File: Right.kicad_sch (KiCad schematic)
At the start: 196 parts, among them J1 USB_C_Receptacle_USB2.0, J2 USB_C_Receptacle_USB2.0, J3 AVR-ISP-6, Q1 DMN2041L, Q2 DMN2041L, SW1 SW_Push, SW10 SW_Push, SW11 SW_Push, SW12 SW_Push, SW13 SW_Push, SW14 SW_Push, SW15 SW_Push, SW17 SW_Push, SW18 SW_Push, SW2 SW_Push, SW20 SW_Push, SW21 SW_Push, SW23 SW_Push, SW24 SW_Push, SW25 SW_Push, SW27 SW_Push, SW28 SW_Push, SW3 SW_Push, SW30 SW_Push, SW31 SW_Push, SW32 SW_Push, SW33 SW_Push, SW34 SW_Push, SW35 SW_Push, SW36 SW_Push, SW37 SW_Push, SW38 SW_Push, SW39 SW_Push, SW4 SW_Push, SW40 SW_Push, SW41 SW_Push, SW42 SW_Push, SW43 SW_Push, SW44 SW_Push, SW45 SW_Push, SW46 SW_Push, SW47 SW_Push, SW5 SW_Push, SW6 SW_Push, SW7 SW_Push, SW8 SW_Push, SW9 SW_Push, U1 ATmega32U4-A, Y1 16MHz

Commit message: replaced LEDs with RGBs, and started the PCB for keyboard
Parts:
- removed C1, C2, C7: .1uF, symbol Device:C_Small
- removed C3, C5: 22pF, symbol Device:C_Small
- removed C4: 1uF, symbol Device:C_Small
- removed C6: 10uf, symbol Device:C_Small
- removed D1, D11, D14, D17, D18, D19, D2, D20, D3, D31, D33, D34, D35, D39, D40, D44, D46, D48, D50, D52, D56, D61, D62, D63, D64, D67, D7, D72, D73, D74, D75, D76, D79, D8, D82, D83, D85, D86, D88, D9, D91: LED, symbol Device:LED
- removed D10, D16, D22, D23, D25, D29, D30, D37, D4, D42, D43, D47, D5, D51, D54, D58, D6, D60, D66, D68, D69, D71, D78, D84, D87, D89, D90: D_Small, symbol Device:D_Small
- removed D21: PRTR5V0U2X, Package_TO_SOT_SMD:SOT-143, symbol Power_Protection:PRTR5V0U2X
- removed F1: 500m, symbol Device:Polyfuse_Small
- removed J1: USB_C_Receptacle_USB2.0, symbol Connector:USB_C_Receptacle_USB2.0
- removed J3: AVR-ISP-6, symbol Connector:AVR-ISP-6
- removed Q1: DMN2041L, Package_TO_SOT_SMD:SOT-23, symbol Transistor_FET:DMN2041L
- removed R1, R11, R12, R13, R14, R15, R17, R18, R19, R20, R24, R25, R27, R28, R29, R3, R30, R33, R35, R36, R37, R38, R39, R4, R40, R41, R42, R43, R45, R46, R47, R48, R49, R5, R50, R52, R53, R54, R6, R7, R9: 470, symbol Device:R_Small
- removed R2, R44: 22, symbol Device:R_Small
- removed R21: 1k, symbol Device:R_Small
- removed R22, R31: 5.1k, symbol Device:R_Small
- removed R23, R34: 10k, symbol Device:R_Small
- removed SW1, SW12, SW15, SW18, SW2, SW20, SW24, SW27, SW3, SW31, SW32, SW34, SW35, SW37, SW39, SW4, SW41, SW42, SW43, SW44, SW46, SW47, SW5, SW6, SW7, SW8, SW9: SW_Push, keyswitches.pretty-2:Kailh_socket_PG1350, symbol Switch:SW_Push
- removed SW28: SW_Push, Button_Switch_SMD:SW_SPST_SKQG_WithStem, symbol Switch:SW_Push
- removed Y1: 16MHz, symbol Device:Crystal_GND24_Small
- added C301, C302: 22pF, Capacitor_SMD:C_0402_1005Metric, symbol Device:C_Small
- added C303: 1uF, Capacitor_SMD:C_0402_1005Metric, symbol Device:C_Small
- added C304, C305, C306: .1uF, Capacitor_SMD:C_0402_1005Metric, symbol Device:C_Small
- added C307: 10uf, Capacitor_SMD:C_0402_1005Metric, symbol Device:C_Small
- added C308, C309, C310, C311, C312, C313, C314, C315, C316, C317, C318, C319, C320, C321, C322, C323, C324, C325, C326, C327, C328, C329, C330, C331, C332, C333, C334, C335, C336, C337, C338, C339, C340, C341, C342, C343, C344, C345, C346, C347, C348: 100nF, Capacitor_SMD:C_0402_1005Metric, symbol Device:C_Small
- added D302: PRTR5V0U2X, Package_TO_SOT_SMD:SOT-143, symbol Power_Protection:PRTR5V0U2X
- added D303, D304, D305, D306, D307, D308, D309, D310, D311, D312, D313, D314, D315, D316, D317, D318, D319, D320, D321, D322, D323, D324, D325, D326, D327, D328, D329, D330, D331, D332, D333, D334, D335, D336, D337, D338, D339, D340, D341, D342, D343: NeoPixel_THT, kicad-keyboard-parts.pretty:LED_RGB_Wuerth-PLCC4_3.2x2.8mm_150141M173100, symbol LED:NeoPixel_THT
- added D346, D347, D349, D350, D351, D352, D353, D354, D355, D356, D357, D358, D359, D360, D362, D374, D375, D376, D377, D378, D379, D380, D381, D382, D383, D384, D385: D_Small, Diode_SMD:D_SOD-123, symbol Device:D_Small
- added F301: 500m, Keebio-Parts:Fuse_0805, symbol Device:Polyfuse_Small
- added FB301: FerriteBead_Small, Inductor_SMD:L_0805_2012Metric_Pad1.15x1.40mm_HandSolder, symbol Device:FerriteBead_Small
- added H301, H302, H303, H304, H305, H306: MountingHole, MountingHole:MountingHole_2.2mm_M2_DIN965_Pad, symbol Mechanical:MountingHole
- added J302: USB_C_Receptacle_USB2.0, Type-C:HRO-TYPE-C-31-M-13, symbol Connector:USB_C_Receptacle_USB2.0
- added J303: AVR-ISP-6, Keebio-Parts:ICSP-Header, symbol Connector:AVR-ISP-6
- added R302, R304: 5.1k, Resistor_SMD:R_0402_1005Metric, symbol Device:R_Small
- added R305: 300, Resistor_SMD:R_0402_1005Metric, symbol Device:R_Small
- added R323, R327: 22, Resistor_SMD:R_0402_1005Metric, symbol Device:R_Small
- added R328, R341: 10k, Resistor_SMD:R_0402_1005Metric, symbol Device:R_Small
- added SW301: SW_Push, Button_Switch_SMD:SW_SPST_SKQG_WithStem, symbol Switch:SW_Push
- added SW304, SW305, SW307, SW308, SW309, SW311, SW312, SW313, SW314, SW316, SW317, SW318, SW320, SW331, SW332, SW333, SW336, SW337, SW338, SW339, SW340, SW341, SW342: SW_Push, keyswitches.pretty-2:Kailh_socket_PG1350, symbol Switch:SW_Push
- added SW310, SW335: SW_Push, keyswitches.pretty-2:Kailh_socket_PG1350_2.25U, symbol Switch:SW_Push
- added SW315: SW_Push, keyswitches.pretty-2:Kailh_socket_PG1350_1.25U, symbol Switch:SW_Push
- added SW334: SW_Push, keyswitches.pretty-2:Kailh_socket_PG1350_1.5U, symbol Switch:SW_Push
- added Y301: 16MHz, Crystal:Crystal_SMD_3225-4Pin_3.2x2.5mm, symbol Device:Crystal_GND24_Small
- D344: renamed from D15; footprint (none) -> Diode_SMD:D_SOD-123
- D345: renamed from D81; footprint (none) -> Diode_SMD:D_SOD-123
- D348: renamed from D12; footprint (none) -> Diode_SMD:D_SOD-123
- D361: renamed from D45; footprint (none) -> Diode_SMD:D_SOD-123
- D363: renamed from D41; footprint (none) -> Diode_SMD:D_SOD-123
- D364: renamed from D26; footprint (none) -> LED_SMD:LED_PLCC_2835
- D365: renamed from D70; footprint (none) -> Diode_SMD:D_SOD-123
- D366: renamed from D27; footprint (none) -> Diode_SMD:D_SOD-123
- D367: renamed from D57; footprint (none) -> Diode_SMD:D_SOD-123
- D368: renamed from D28; footprint (none) -> Diode_SMD:D_SOD-123
- D369: renamed from D80; footprint (none) -> Diode_SMD:D_SOD-123
- D370: renamed from D49; footprint (none) -> Diode_SMD:D_SOD-123
- D371: renamed from D77; footprint (none) -> Diode_SMD:D_SOD-123
- D372: renamed from D13; footprint (none) -> Diode_SMD:D_SOD-123
- D373: renamed from D24; footprint (none) -> Diode_SMD:D_SOD-123
- J301: renamed from J2; footprint (none) -> Type-C:HRO-TYPE-C-31-M-13
- R301: renamed from R32; footprint (none) -> Resistor_SMD:R_0402_1005Metric
- R303: renamed from R51; footprint (none) -> Resistor_SMD:R_0402_1005Metric
- R345: renamed from R26; footprint (none) -> Resistor_SMD:R_0402_1005Metric
- R346: renamed from R16; footprint (none) -> Resistor_SMD:R_0402_1005Metric
- R353: renamed from R8; footprint (none) -> Resistor_SMD:R_0402_1005Metric
- R354: renamed from R10; footprint (none) -> Resistor_SMD:R_0402_1005Metric
- SW329: renamed from SW36; footprint keyswitches.pretty-2:Kailh_socket_PG1350 -> keyswitches.pretty-2:Kailh_socket_PG1350_1.75U
- gave numbers to parts that had none: 1
- renumbered Q2 to Q302, SW25 to SW302, SW23 to SW303, SW13 to SW306, SW38 to SW319, SW11 to SW321, SW33 to SW322, SW10 to SW323, SW17 to SW324, SW14 to SW325, SW45 to SW326, SW21 to SW327, SW30 to SW328, SW40 to SW330, U1 to U301
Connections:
- net +5V: now also C304.1, C305.1, C306.1, C307.1, C308.2, C309.2, C310.2, C311.2, C312.1, C312.2, C313.2, C314.2, C315.2, C316.2, C317.2, C318.2, C319.2, C320.2, C321.2, C322.2, C323.2, C324.2, C325.2, C326.2, C327.2, C328.2, C329.2, C330.2, C331.2, C332.2, C333.2, C334.2, C335.2, C336.2, C337.2, C338.2, C339.2, C340.2, C341.2, C342.2, C343.2, C344.2, C345.2, C346.2, C347.1, C347.2, C348.2, D303.3 (VDD), D304.3 (VDD), D305.3 (VDD), D306.3 (VDD), D307.3 (VDD), D308.3 (VDD), D309.3 (VDD), D310.3 (VDD), D311.3 (VDD), D312.3 (VDD), D313.3 (VDD), D314.3 (VDD), D315.3 (VDD), D316.3 (VDD), D317.3 (VDD), D318.3 (VDD), D319.3 (VDD), D320.3 (VDD), D321.3 (VDD), D322.3 (VDD), D323.3 (VDD), D324.3 (VDD), D325.3 (VDD), D326.3 (VDD), D327.3 (VDD), D328.3 (VDD), D329.3 (VDD), D330.3 (VDD), D331.3 (VDD), D332.3 (VDD), D333.3 (VDD), D334.2 (GND), D334.3 (VDD), D335.3 (VDD), D336.3 (VDD), D337.3 (VDD), D338.3 (VDD), D339.3 (VDD), D340.3 (VDD), D341.3 (VDD), D342.3 (VDD), D343.3 (VDD), F301.2, J303.2 (VCC), R328.1
- net COL_0: now also SW304.2, SW305.2
- net COL_1: now also SW307.2, SW308.2, SW309.2, SW310.2
- net COL_2: now also SW311.2, SW312.2, SW313.2, SW314.2, SW315.2
- net COL_3: now also SW316.2, SW317.2, SW318.2, SW320.2
- net D+: now also D302.3 (I/O2), J302.A6 (D+), J302.B6 (D+), R327.1
- net D-: now also D302.2 (I/O1), J302.A7 (D-), J302.B7 (D-), R323.1
- net DATA_2: now also D301.2 (I/O1)
- net GND: now also C301.1, C302.2, C303.2, C304.2, C305.2, C306.2, C307.2, C308.1, C309.1, C310.1, C311.1, C313.1, C314.1, C315.1, C316.1, C317.1, C318.1, C319.1, C320.1, C321.1, C322.1, C323.1, C324.1, C325.1, C326.1, C327.1, C328.1, C329.1, C330.1, C331.1, C332.1, C333.1, C334.1, C335.1, C336.1, C337.1, C338.1, C339.1, C340.1, C341.1, C342.1, C343.1, C344.1, C345.1, C346.1, C348.1, D302.1 (GND), D303.2 (GND), D304.2 (GND), D305.2 (GND), D306.2 (GND), D307.2 (GND), D308.2 (GND), D309.2 (GND), D310.2 (GND), D311.2 (GND), D312.2 (GND), D313.2 (GND), D314.2 (GND), D315.2 (GND), D316.2 (GND), D317.2 (GND), D318.2 (GND), D319.2 (GND), D320.2 (GND), D321.2 (GND), D322.2 (GND), D323.2 (GND), D324.2 (GND), D325.2 (GND), D326.2 (GND), D327.2 (GND), D328.2 (GND), D329.2 (GND), D330.2 (GND), D331.2 (GND), D332.2 (GND), D333.2 (GND), D335.2 (GND), D336.2 (GND), D337.2 (GND), D338.2 (GND), D339.2 (GND), D340.2 (GND), D341.2 (GND), D342.2 (GND), D343.2 (GND), FB301.2, J302.A1 (GND), J302.A12 (GND), J302.B1 (GND), J302.B12 (GND), J303.6 (GND), R302.2, R304.2, R341.2, SW301.1, Y301.2, Y301.4
- net MISO: now also J303.1 (MISO)
- net MOSI: now also J303.4 (MOSI)
- net ROW_0: now also D352.1 (K), D357.1 (K), D362.1 (K), D380.1 (K), D385.1 (K)
- net ROW_1: now also D347.1 (K), D351.1 (K), D356.1 (K), D379.1 (K), D384.1 (K)
- net ROW_2: now also D346.1 (K), D350.1 (K), D355.1 (K), D360.1 (K), D378.1 (K), D383.1 (K)
- net ROW_3: now also D349.1 (K), D354.1 (K), D359.1 (K), D375.1 (K), D377.1 (K), D382.1 (K)
- net ROW_4: now also D353.1 (K), D358.1 (K), D374.1 (K), D376.1 (K), D381.1 (K)
- net RST: now also J303.5 (~{RST}), R328.2, SW301.2
- net SCLK: now also J303.3 (SCK)
- net VCC: now also D302.4 (VCC), F301.1, J302.A4 (VBUS), J302.A9 (VBUS), J302.B4 (VBUS), J302.B9 (VBUS)
- net at U301.16 (XTAL2): now also C302.1, Y301.3
- net at U301.17 (XTAL1): now also C301.2, Y301.1
- net COL_8: now reaches U301.19 (PD1)
- net COL_8: now also SW338.2, SW339.2, SW340.2, SW341.2, SW342.2
- net D_N: now reaches U301.3 (D-)
- net D_N: now also R323.2
- net at U301.33 (~{HWB}/PE2): now also R341.1
- net D_P: now reaches U301.4 (D+)
- net D_P: now also R327.2
- net at U301.6 (UCAP): now also C303.1
- net PWM: no longer names the net of U301.12 (PB7)
- net PWM: now also R305.1
- net ROW_5 renamed COL_6
- net COL_6: now also SW331.2, SW332.2
- net ROW_6 renamed COL_7
- net COL_7: now also SW333.2, SW334.2, SW335.2, SW336.2, SW337.2
- new net: D360.2 (A), SW318.1
- new net: D353.2 (A), SW311.1
- new net: D376.2 (A), SW333.1
- new net: D331.1 (DOUT), D332.4 (DIN)
- new net: D330.1 (DOUT), D331.4 (DIN)
- new net: D362.2 (A), SW320.1
- new net: D338.1 (DOUT), D339.4 (DIN)
- new net: D337.1 (DOUT), D338.4 (DIN)
- new net: J302.A5 (CC1), R304.1
- new net: D319.1 (DOUT), D320.4 (DIN)
- new net: D354.2 (A), SW312.1
- new net: J302.B5 (CC2), R302.1
- new net: D377.2 (A), SW334.1
- new net: D381.2 (A), SW338.1
- new net: D358.2 (A), SW316.1
- new net: D352.2 (A), SW310.1
- new net: D351.2 (A), SW309.1
- new net: D355.2 (A), SW313.1
- new net: D384.2 (A), SW341.1
- new net: D307.1 (DOUT), D308.4 (DIN)
- new net: D306.1 (DOUT), D307.4 (DIN)
- new net: D349.2 (A), SW307.1
- new net: D312.1 (DOUT), D313.4 (DIN)
- new net: D311.1 (DOUT), D312.4 (DIN)
- new net: D329.1 (DOUT), D330.4 (DIN)
- new net: D346.2 (A), SW304.1
- new net: D339.1 (DOUT), D340.4 (DIN)
- new net: D357.2 (A), SW315.1
- new net: D336.1 (DOUT), D337.4 (DIN)
- new net: D340.1 (DOUT), D341.4 (DIN)
- new net: D350.2 (A), SW308.1
- new net: D322.1 (DOUT), D323.4 (DIN)
- new net: D321.1 (DOUT), D322.4 (DIN)
- new net: D382.2 (A), SW339.1
- new net: D359.2 (A), SW317.1
- new net: D378.2 (A), SW335.1
- new net: D380.2 (A), SW337.1
- new net: D305.1 (DOUT), D306.4 (DIN)
- new net: D309.1 (DOUT), D310.4 (DIN)
- new net: D308.1 (DOUT), D309.4 (DIN)
- new net: D385.2 (A), SW342.1
- new net: D315.1 (DOUT), D316.4 (DIN)
- new net: D314.1 (DOUT), D315.4 (DIN)
- new net: D317.1 (DOUT), D318.4 (DIN)
- new net: D316.1 (DOUT), D317.4 (DIN)
- new net: D383.2 (A), SW340.1
- new net: D335.1 (DOUT), D336.4 (DIN)
- new net: D325.1 (DOUT), D326.4 (DIN)
- new net: D324.1 (DOUT), D325.4 (DIN)
- new net: D356.2 (A), SW314.1
- new net: D320.1 (DOUT), D321.4 (DIN)
- new net: D328.1 (DOUT), D329.4 (DIN)
- new net: D327.1 (DOUT), D328.4 (DIN)
- new net: D379.2 (A), SW336.1
- new net: D303.1 (DOUT), D304.4 (DIN)
- new net: D341.1 (DOUT), D342.4 (DIN)
- new net: D374.2 (A), SW331.1
- new net: D313.1 (DOUT), D314.4 (DIN)
- new net: D347.2 (A), SW305.1
- new net: D323.1 (DOUT), D324.4 (DIN)
- new net: D333.1 (DOUT), D334.4 (DIN)
- new net: D332.1 (DOUT), D333.4 (DIN)
- new net: D304.1 (DOUT), D305.4 (DIN)
- new net: D375.2 (A), SW332.1
- new net D211: D310.1 (DOUT), D311.4 (DIN)
- new net D219: D318.1 (DOUT), D319.4 (DIN)
- new net D227: D326.1 (DOUT), D327.4 (DIN)
- new net D235: D334.1 (DOUT), D335.4 (DIN)
- new net D303: D303.4 (DIN), D343.1 (DOUT)
- new net Earth: FB301.1, J302.S1 (SHIELD)
- new net RGB: D343.4 (DIN), R305.2
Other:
- note added: "41 RGB LEDs Matrix"
- note removed: "41 LEDs"
- moved on the sheet: D301, D344, D345, D348, D361, D363, D365, D366, D367, D368, D369, D370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

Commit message: did some more work on the keyboard, played around with the rotary footprint
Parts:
- SW301: footprint Button_Switch_SMD:SW_SPST_SKQG_WithStem -> Keebio-Parts:SW_SPST_TL3342
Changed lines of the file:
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@@
     (property "Reference" "SW301" (id 0) (at 190.5 76.2 0))
     (property "Value" "SW_Push" (id 1) (at 190.5 78.74 0))
-    (property "Footprint" "Button_Switch_SMD:SW_SPST_SKQG_WithStem" (id 2) (at 190.5 78.74 0)
+    (property "Footprint" "Keebio-Parts:SW_SPST_TL3342" (id 2) (at 190.5 78.74 0)
       (effects (font (size 1.27 1.27)) hide)
     )

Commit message: did some routing
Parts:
- removed D301: PRTR5V0U2X, Package_TO_SOT_SMD:SOT-143, symbol Power_Protection:PRTR5V0U2X
- removed D364: LED, LED_SMD:LED_PLCC_2835, symbol Device:LED
- removed J301: USB_C_Receptacle_USB2.0, Type-C:HRO-TYPE-C-31-M-13, symbol Connector:USB_C_Receptacle_USB2.0
- removed Q302: DMN2041L, Package_TO_SOT_SMD:SOT-23, symbol Transistor_FET:DMN2041L
- removed R301, R303: 5.1k, Resistor_SMD:R_0402_1005Metric, symbol Device:R_Small
- removed R345, R346: 4.7K, Resistor_SMD:R_0402_1005Metric, symbol Device:R_Small
- removed R353: 470, Resistor_SMD:R_0402_1005Metric, symbol Device:R_Small
- removed R354: 1k, Resistor_SMD:R_0402_1005Metric, symbol Device:R_Small
- added R1, R2: 4.7K, Resistor_SMD:R_0402_1005Metric, symbol Device:R_Small
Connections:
- net +5V: now also R1.2, R2.2
- net DATA_1: now also U301.20 (PD2), R2.1
- net DATA_2: now also U301.21 (PD3), R1.1
- no-connect marks 10 -> 8
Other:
- note removed: "CAPS LOCK LED"

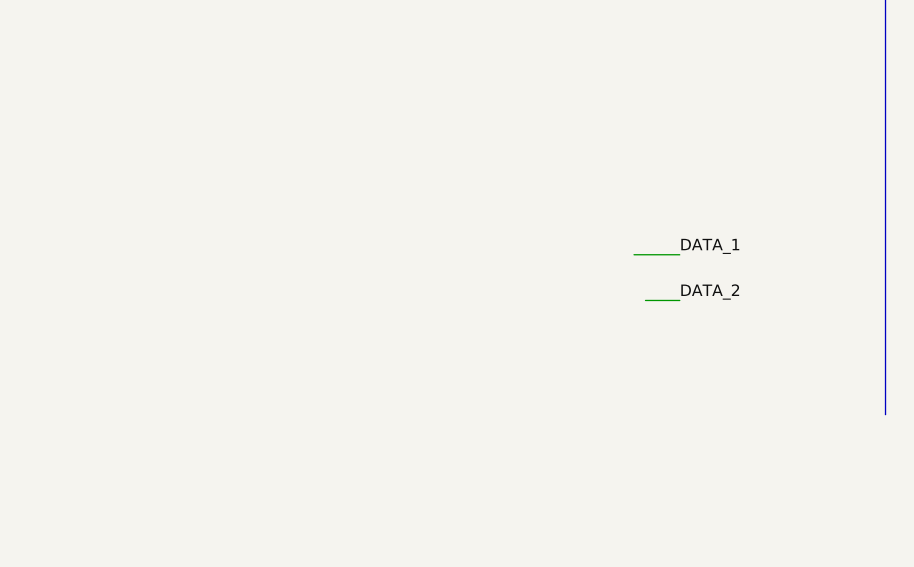
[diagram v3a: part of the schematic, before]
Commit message: placed some i2cs
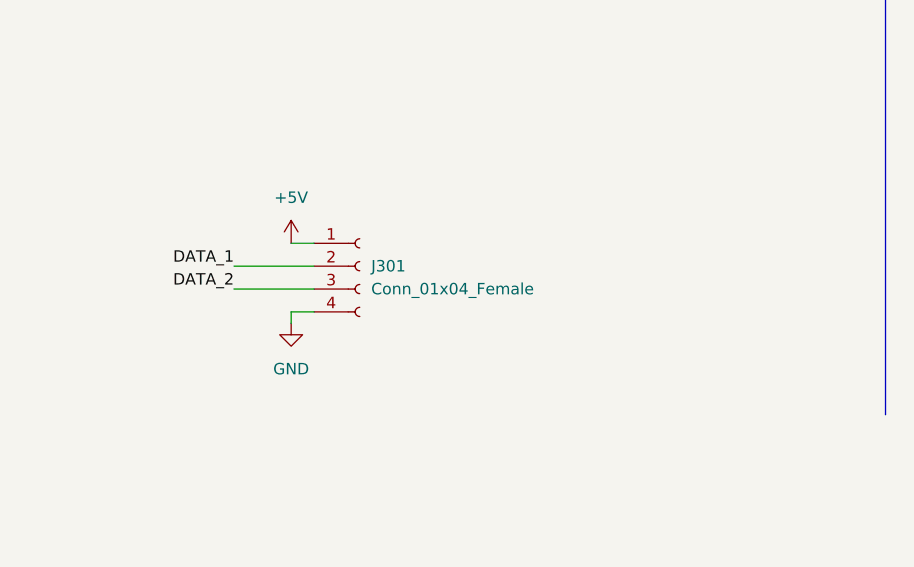
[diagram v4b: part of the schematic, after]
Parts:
- added J301: Conn_01x04_Female, Keebio-Parts:I2C_Breakout, symbol Connector:Conn_01x04_Female
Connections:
- net +5V: now also J301.1 (Pin_1)
- net DATA_1: now also J301.2 (Pin_2)
- net DATA_2: now also J301.3 (Pin_3)
- net GND: now also J301.4 (Pin_4)
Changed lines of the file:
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@@
     (stroke (width 0) (type default) (color 0 0 0 0))
   )
+  (wire (pts (xy 246.38 215.9) (xy 248.92 215.9))
+    (stroke (width 0) (type default) (color 0 0 0 0))
+  )
   (wire (pts (xy 62.23 187.96) (xy 69.85 187.96))
     (stroke (width 0) (type default) (color 0 0 0 0))
@@
     (stroke (width 0) (type default) (color 0 0 0 0))
   )
+  (wire (pts (xy 246.38 223.52) (xy 248.92 223.52))
+    (stroke (width 0) (type default) (color 0 0 0 0))
+  )
   (wire (pts (xy 129.54 170.18) (xy 130.81 170.18))
     (stroke (width 0) (type default) (color 0 0 0 0))
@@
     (stroke (width 0) (type default) (color 0 0 0 0))
   )
-  (wire (pts (xy 289.56 217.17) (xy 284.48 217.17))
+  (wire (pts (xy 240.03 218.44) (xy 248.92 218.44))
+    (stroke (width 0) (type default) (color 0 0 0 0))
+  )
+  (wire (pts (xy 246.38 223.52) (xy 246.38 224.79))
     (stroke (width 0) (type default) (color 0 0 0 0))
   )
@@
     (stroke (width 0) (type default) (color 0 0 0 0))
   )
-  (wire (pts (xy 289.56 222.25) (xy 285.75 222.25))
+  (wire (pts (xy 240.03 220.98) (xy 248.92 220.98))
     (stroke (width 0) (type default) (color 0 0 0 0))
   )
@@
     (effects (font (size 1.27 1.27)) (justify right bottom))
   )
-  (label "DATA_1" (at 289.56 217.17 0)
-    (effects (font (size 1.27 1.27)) (justify left bottom))
+  (label "DATA_1" (at 240.03 218.44 180)
+    (effects (font (size 1.27 1.27)) (justify right bottom))
   )
   (label "D211" (at 181.61 156.21 0)
@@
     (effects (font (size 1.27 1.27)) (justify left bottom))
   )
-  (label "DATA_2" (at 289.56 222.25 0)
-    (effects (font (size 1.27 1.27)) (justify left bottom))
+  (label "DATA_2" (at 240.03 220.98 180)
+    (effects (font (size 1.27 1.27)) (justify right bottom))
   )
   (label "COL_7" (at 388.62 152.4 270)
@@
     (pin "2")
   )
+  (symbol (lib_id "Connector:Conn_01x04_Female") (at 254 218.44 0) (unit 1)
+    (in_bom yes) (on_board yes) (fields_autoplaced)
+    (property "Reference" "J301" (id 0) (at 255.27 218.4399 0)
+      (effects (font (size 1.27 1.27)) (justify left))
+    )
+    (property "Value" "Conn_01x04_Female" (id 1) (at 255.27 220.9799 0)
+      (effects (font (size 1.27 1.27)) (justify left))
+    )
+    (property "Footprint" "Keebio-Parts:I2C_Breakout" (id 2) (at 254 218.44 0)
+      (effects (font (size 1.27 1.27)) hide)
+    )
+    (property "Datasheet" "~" (id 3) (at 254 218.44 0)
+      (effects (font (size 1.27 1.27)) hide)
+    )
+    (pin "1")
+    (pin "2")
+    (pin "3")
+    (pin "4")
+  )
   (symbol (lib_id "Device:C_Small") (at 66.04 170.18 90) (unit 1)
     (in_bom yes) (on_board yes) (fields_autoplaced)
@@
     (pin "2")
   )
+  (symbol (lib_id "power:GND") (at 246.38 224.79 0) (unit 1)
+    (in_bom yes) (on_board yes) (fields_autoplaced)
+    (property "Reference" "#PWR0303" (id 0) (at 246.38 231.14 0)
+      (effects (font (size 1.27 1.27)) hide)
+    )
+    (property "Value" "GND" (id 1) (at 246.38 229.87 0))
+    (property "Footprint" "" (id 2) (at 246.38 224.79 0)
+      (effects (font (size 1.27 1.27)) hide)
+    )
+    (property "Datasheet" "" (id 3) (at 246.38 224.79 0)
+      (effects (font (size 1.27 1.27)) hide)
+    )
+    (pin "1")
+  )
   (symbol (lib_id "Device:D_Small") (at 278.13 124.46 90) (unit 1)
     (in_bom yes) (on_board yes) (fields_autoplaced)
@@
       (effects (font (size 1.27 1.27)) hide)
     )
+    (pin "1")
+  )
+  (symbol (lib_id "power:+5V") (at 246.38 215.9 0) (unit 1)
+    (in_bom yes) (on_board yes) (fields_autoplaced)
+    (property "Reference" "#PWR0301" (id 0) (at 246.38 219.71 0)
+      (effects (font (size 1.27 1.27)) hide)
+    )
+    (property "Value" "+5V" (id 1) (at 246.38 210.82 0))
+    (property "Footprint" "" (id 2) (at 246.38 215.9 0)
+      (effects (font (size 1.27 1.27)) hide)
+    )
+    (property "Datasheet" "" (id 3) (at 246.38 215.9 0)
+      (effects (font (size 1.27 1.27)) hide)
+    )

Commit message: did some more routing
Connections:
- net COL_0: now also U301.22 (PD5); no longer U301.41 (PF0)
- net COL_1: now also U301.19 (PD1); no longer U301.40 (PF1)
- net COL_2: now also U301.18 (PD0); no longer U301.39 (PF4)
- net COL_3: now also U301.12 (PB7); no longer U301.38 (PF5)
- net COL_4: no longer U301.37 (PF6)
- net COL_5: no longer U301.36 (PF7)
- net COL_6: now also U301.1 (PE6); no longer U301.29 (PB5)
- net COL_8: no longer U301.19 (PD1)
- net ROW_0: no longer U301.22 (PD5)
- net at R305.1: now also U301.8 (PB0); no longer U301.12 (PB7)
- net CAPS_LOCK_PWM: no longer names the net of U301.31 (PC6)
- no-connect marks 8 -> 4
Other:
- moved on the sheet: R305

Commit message: whole lot of routing
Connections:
- net +5V: no longer C312.1
- net GND: now also C312.1
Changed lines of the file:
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@@
   (junction (at 82.55 233.68) (diameter 0) (color 0 0 0 0)
+  )
+  (junction (at 101.6 165.1) (diameter 0) (color 0 0 0 0)
   )
   (junction (at 303.53 142.24) (diameter 0) (color 0 0 0 0)
@@
     (stroke (width 0) (type default) (color 0 0 0 0))
   )
+  (wire (pts (xy 104.14 147.32) (xy 101.6 147.32))
+    (stroke (width 0) (type default) (color 0 0 0 0))
+  )
   (wire (pts (xy 391.16 128.27) (xy 406.4 128.27))
     (stroke (width 0) (type default) (color 0 0 0 0))
@@
     (stroke (width 0) (type default) (color 0 0 0 0))
   )
+  (wire (pts (xy 101.6 165.1) (xy 102.87 165.1))
+    (stroke (width 0) (type default) (color 0 0 0 0))
+  )
   (wire (pts (xy 292.1 138.43) (xy 306.07 138.43))
     (stroke (width 0) (type default) (color 0 0 0 0))
@@
     (stroke (width 0) (type default) (color 0 0 0 0))
   )
+  (wire (pts (xy 101.6 147.32) (xy 101.6 165.1))
+    (stroke (width 0) (type default) (color 0 0 0 0))
+  )
   (wire (pts (xy 388.62 101.6) (xy 388.62 111.76))
     (stroke (width 0) (type default) (color 0 0 0 0))
@@
     (stroke (width 0) (type default) (color 0 0 0 0))
   )
-  (wire (pts (xy 90.17 165.1) (xy 102.87 165.1))
+  (wire (pts (xy 90.17 165.1) (xy 101.6 165.1))
     (stroke (width 0) (type default) (color 0 0 0 0))
   )
@@
     (stroke (width 0) (type default) (color 0 0 0 0))
   )
-  (wire (pts (xy 90.17 147.32) (xy 104.14 147.32))
-    (stroke (width 0) (type default) (color 0 0 0 0))
-  )

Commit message: did a bunch of routing
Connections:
- net COL_0: now also U301.38 (PF5); no longer U301.22 (PD5)
- net COL_1: now also U301.37 (PF6); no longer U301.19 (PD1)
- net COL_2: now also U301.36 (PF7); no longer U301.18 (PD0)
- net COL_3: now also U301.31 (PC6); no longer U301.12 (PB7)
- net COL_4: now also U301.32 (PC7)
- net COL_5: now also U301.12 (PB7)
- net COL_8: now also U301.29 (PB5)
- net ROW_0: now also U301.39 (PF4)
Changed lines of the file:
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@@
     (stroke (width 0) (type default) (color 0 0 0 0))
   )
-  (wire (pts (xy 233.68 101.6) (xy 231.14 101.6))
+  (wire (pts (xy 231.14 101.6) (xy 233.68 101.6))
     (stroke (width 0) (type default) (color 0 0 0 0))
   )
@@
     (stroke (width 0) (type default) (color 0 0 0 0))
   )
-  (wire (pts (xy 238.76 106.68) (xy 236.22 106.68))
-    (stroke (width 0) (type default) (color 0 0 0 0))
-  )
   (wire (pts (xy 29.21 166.37) (xy 49.53 166.37))
     (stroke (width 0) (type default) (color 0 0 0 0))
@@
     (stroke (width 0) (type default) (color 0 0 0 0))
   )
-  (wire (pts (xy 233.68 116.84) (xy 231.14 116.84))
-    (stroke (width 0) (type default) (color 0 0 0 0))
-  )
   (wire (pts (xy 278.13 127) (xy 278.13 128.27))
     (stroke (width 0) (type default) (color 0 0 0 0))
@@
     (stroke (width 0) (type default) (color 0 0 0 0))
   )
+  (wire (pts (xy 233.68 157.48) (xy 231.14 157.48))
+    (stroke (width 0) (type default) (color 0 0 0 0))
+  )
   (wire (pts (xy 320.04 137.16) (xy 320.04 138.43))
     (stroke (width 0) (type default) (color 0 0 0 0))
@@
     (stroke (width 0) (type default) (color 0 0 0 0))
   )
-  (wire (pts (xy 233.68 114.3) (xy 231.14 114.3))
-    (stroke (width 0) (type default) (color 0 0 0 0))
-  )
   (wire (pts (xy 344.17 111.76) (xy 345.44 111.76))
     (stroke (width 0) (type default) (color 0 0 0 0))
@@
     (stroke (width 0) (type default) (color 0 0 0 0))
   )
-  (wire (pts (xy 233.68 127) (xy 231.14 127))
-    (stroke (width 0) (type default) (color 0 0 0 0))
-  )
   (wire (pts (xy 345.44 142.24) (xy 345.44 152.4))
     (stroke (width 0) (type default) (color 0 0 0 0))
@@
     (stroke (width 0) (type default) (color 0 0 0 0))
   )
-  (wire (pts (xy 256.54 132.08) (xy 254 132.08))
-    (stroke (width 0) (type default) (color 0 0 0 0))
-  )
-  (wire (pts (xy 255.27 154.94) (xy 252.73 154.94))
+  (wire (pts (xy 233.68 96.52) (xy 231.14 96.52))
+    (stroke (width 0) (type default) (color 0 0 0 0))
+  )
+  (wire (pts (xy 233.68 149.86) (xy 231.14 149.86))
     (stroke (width 0) (type default) (color 0 0 0 0))
   )
@@
     (stroke (width 0) (type default) (color 0 0 0 0))
   )
-  (wire (pts (xy 239.8902 151.1421) (xy 237.3502 151.1421))
-    (stroke (width 0) (type default) (color 0 0 0 0))
-  )
   (wire (pts (xy 130.81 212.09) (xy 130.81 215.9))
     (stroke (width 0) (type default) (color 0 0 0 0))
@@
     (stroke (width 0) (type default) (color 0 0 0 0))
   )
+  (wire (pts (xy 233.68 109.22) (xy 231.14 109.22))
+    (stroke (width 0) (type default) (color 0 0 0 0))
+  )
   (wire (pts (xy 233.68 132.08) (xy 231.14 132.08))
     (stroke (width 0) (type default) (color 0 0 0 0))
@@
     (stroke (width 0) (type default) (color 0 0 0 0))
   )
+  (wire (pts (xy 233.68 154.94) (xy 231.14 154.94))
+    (stroke (width 0) (type default) (color 0 0 0 0))
+  )
   (wire (pts (xy 20.32 140.97) (xy 20.32 147.32))
     (stroke (width 0) (type default) (color 0 0 0 0))
@@
     (stroke (width 0) (type default) (color 0 0 0 0))
   )
+  (wire (pts (xy 233.68 106.68) (xy 231.14 106.68))
+    (stroke (width 0) (type default) (color 0 0 0 0))
+  )
   (wire (pts (xy 377.19 128.27) (xy 391.16 128.27))
     (stroke (width 0) (type default) (color 0 0 0 0))
@@
   )
   (wire (pts (xy 109.22 170.18) (xy 110.49 170.18))
+    (stroke (width 0) (type default) (color 0 0 0 0))
+  )
+  (wire (pts (xy 233.68 152.4) (xy 231.14 152.4))
     (stroke (width 0) (type default) (color 0 0 0 0))
   )
@@
     (effects (font (size 1.27 1.27)) (justify left bottom))
   )
-  (label "COL_2" (at 233.68 114.3 0)
-    (effects (font (size 1.27 1.27)) (justify left bottom))
-  )
-  (label "COL_3" (at 233.68 101.6 0)
-    (effects (font (size 1.27 1.27)) (justify left bottom))
-  )
   (label "COL_1" (at 303.53 152.4 270)
     (effects (font (size 1.27 1.27)) (justify right bottom))
@@
     (effects (font (size 1.27 1.27)) (justify left bottom))
   )
-  (label "ROW_0" (at 255.27 154.94 0)
+  (label "ROW_0" (at 233.68 149.86 0)
     (effects (font (size 1.27 1.27)) (justify left bottom))
   )
@@
   )
   (label "D+" (at 87.63 46.99 0)
-    (effects (font (size 1.27 1.27)) (justify left bottom))
-  )
-  (label "COL_0" (at 233.68 127 0)
     (effects (font (size 1.27 1.27)) (justify left bottom))
   )
@@
     (effects (font (size 1.27 1.27)) (justify right bottom))
   )
+  (label "COL_2" (at 233.68 157.48 0)
+    (effects (font (size 1.27 1.27)) (justify left bottom))
+  )
   (label "MISO" (at 195.58 33.02 0)
     (effects (font (size 1.27 1.27)) (justify left bottom))
@@
     (effects (font (size 1.27 1.27)) (justify left bottom))
   )
+  (label "COL_0" (at 233.68 152.4 0)
+    (effects (font (size 1.27 1.27)) (justify left bottom))
+  )
+  (label "COL_1" (at 233.68 154.94 0)
+    (effects (font (size 1.27 1.27)) (justify left bottom))
+  )
   (label "COL_3" (at 331.47 152.4 270)
     (effects (font (size 1.27 1.27)) (justify right bottom))
@@
     (effects (font (size 1.27 1.27)) (justify right bottom))
   )
+  (label "COL_3" (at 233.68 106.68 0)
+    (effects (font (size 1.27 1.27)) (justify left bottom))
+  )
   (label "D_P" (at 198.12 109.22 90)
     (effects (font (size 1.27 1.27)) (justify left bottom))
@@
     (effects (font (size 1.27 1.27)) (justify right bottom))
   )
-  (label "COL_1" (at 233.68 116.84 0)
-    (effects (font (size 1.27 1.27)) (justify left bottom))
-  )
   (label "DATA_2" (at 254 121.92 0)
     (effects (font (size 1.27 1.27)) (justify left bottom))
@@
     (effects (font (size 1.27 1.27)) (justify left bottom))
   )
-  (label "COL_4" (at 238.76 106.68 0)
+  (label "COL_4" (at 233.68 109.22 0)
     (effects (font (size 1.27 1.27)) (justify left bottom))
   )
@@
     (effects (font (size 1.27 1.27)) (justify left bottom))
   )
-  (label "COL_8" (at 256.54 132.08 0)
+  (label "COL_8" (at 233.68 96.52 0)
     (effects (font (size 1.27 1.27)) (justify left bottom))
   )
@@
     (effects (font (size 1.27 1.27)) (justify right bottom))
   )
-  (label "COL_5" (at 239.8902 151.1421 0)
-    (effects (font (size 1.27 1.27)) (justify left bottom))
-  )
+  (label "COL_5" (at 233.68 101.6 0)
+    (effects (font (size 1.27 1.27)) (justify left bottom))
+  )
